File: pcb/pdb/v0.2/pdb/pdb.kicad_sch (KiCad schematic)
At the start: 29 parts, among them J1 UPDI, J3 Battery, J4 ESC A, J5 ESC B, J6 ESC C, J7 ESC D, J8 UART, J9 MPU, P1 Motor A, P2 Motor B, P3 Motor C, P4 Motor D, SW1 Control, SW2 Reset, U1 ATtiny814-SS, U2 LM317

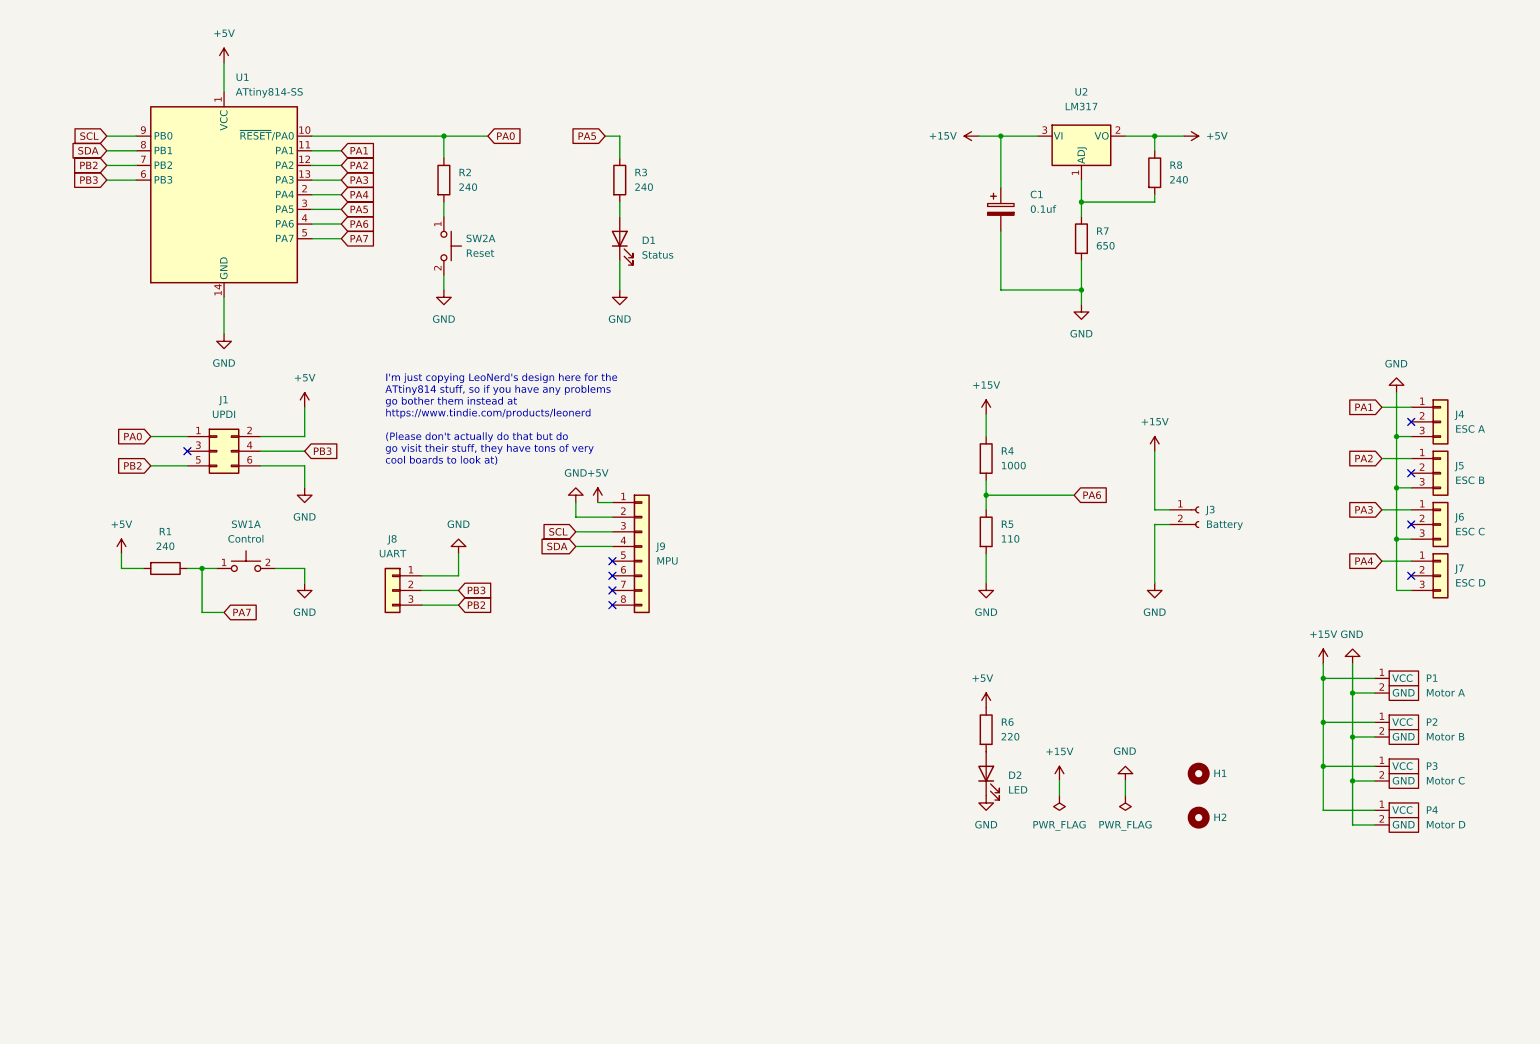
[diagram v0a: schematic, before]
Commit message: pcd: pdb: add USB port
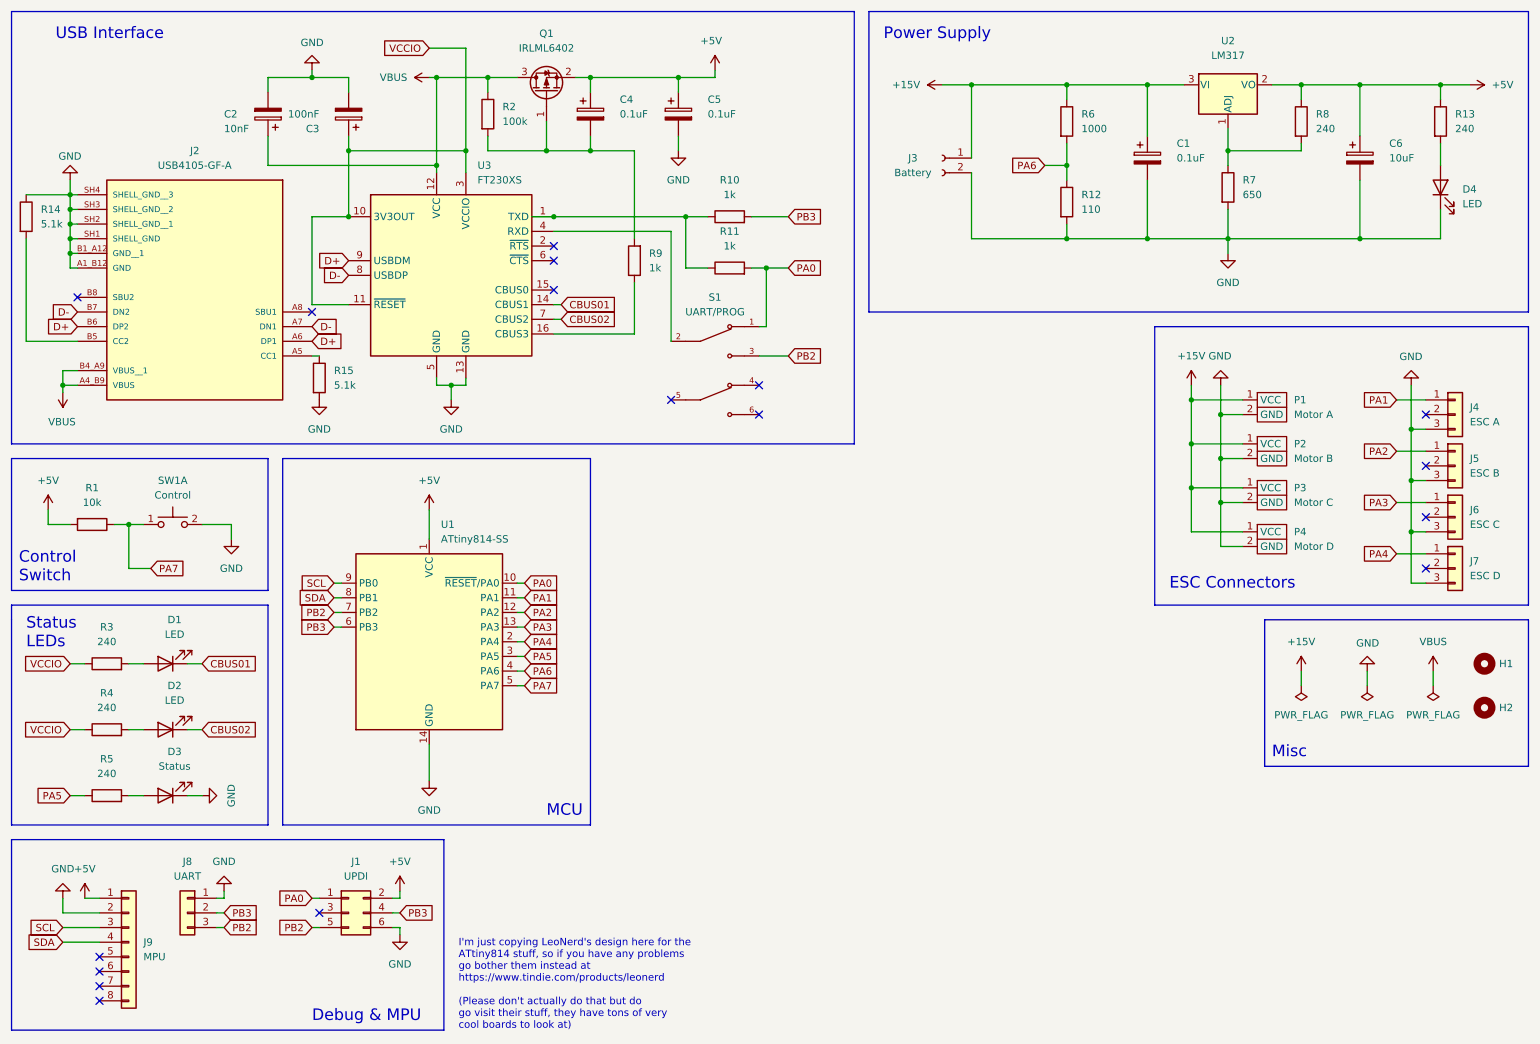
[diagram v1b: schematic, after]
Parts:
- removed SW2: Reset, Button_Switch_THT:SW_PUSH_6mm, symbol Switch:SW_Push_Dual_x2
- added C2: 10nF, Capacitor_SMD:C_1206_3216Metric, symbol Device:C_Polarized
- added C3: 100nF, Capacitor_SMD:C_1206_3216Metric, symbol Device:C_Polarized
- added C4, C5: 0.1uF, Capacitor_SMD:C_1206_3216Metric, symbol Device:C_Polarized
- added C6: 10uF, Capacitor_SMD:C_1206_3216Metric, symbol Device:C_Polarized
- added D3: Status, LED_SMD:LED_0805_2012Metric, symbol Device:LED
- added D4: LED, LED_SMD:LED_0805_2012Metric, symbol Device:LED
- added J2: USB4105-GF-A, USB4105:GCT_USB4105-GF-A, symbol USB4105-GF-A:USB4105-GF-A
- added Q1: IRLML6402, Package_TO_SOT_SMD:SOT-23, symbol Transistor_FET:IRLML6402
- added R10, R11, R9: 1k, Resistor_SMD:R_1206_3216Metric, symbol Device:R
- added R12: 110, Resistor_SMD:R_1206_3216Metric, symbol Device:R
- added R13: 240, Resistor_SMD:R_1206_3216Metric, symbol Device:R
- added R14, R15: 5.1k, Resistor_SMD:R_1206_3216Metric, symbol Device:R
- added S1: UART/PROG, Button_Switch_THT:SW_CuK_JS202011AQN_DPDT_Angled, symbol SLW-23775-5A-N-D:SLW-23775-5A-N-D
- added U3: FT230XS, FT230XS_R:SSOP16-0.635-5X4MM, symbol Interface_USB:FT230XS
- C1: value 0.1uf -> 0.1uF
- D1: value Status -> LED
- R1: value 240 -> 10k
- R2: value 240 -> 100k
- R4: value 1000 -> 240
- R5: value 110 -> 240
- R6: value 220 -> 1000
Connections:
- net +15V: now also R6.1; no longer R4.1
- net +5V: now also C4.1, C5.1, C6.1, Q1.2 (S), R13.1; no longer R6.1
- net GND: now also C2.2, C3.2, C5.2, C6.2, D3.1 (K), D4.1 (K), J2.A1_B12 (GND), J2.B1_A12 (GND__1), J2.SH1 (SHELL_GND), J2.SH2 (SHELL_GND__1), J2.SH3 (SHELL_GND__2), J2.SH4 (SHELL_GND__3), R12.2, R14.1, R15.2, U3.13 (GND), U3.5 (GND); no longer D1.1 (K), D2.1 (K), R5.2
- net PA0: now also R11.2, S1.1; no longer R2.1
- net PA5: now also R5.1; no longer R3.1
- net PA6: now also R6.2, R12.1; no longer R4.2, R5.1
- net PB2: now also S1.3
- net PB3: now also R10.2
- net at D2.2 (A): now also R4.2; no longer R6.2
- net at R2.2: now also C4.2, Q1.1 (G), R9.2
- new net: J2.A5 (CC1), R15.1
- new net: S1.2, U3.4 (RXD)
- new net: R9.1, U3.16 (CBUS3)
- new net: R10.1, R11.1, U3.1 (TXD)
- new net: D3.2 (A), R5.2
- new net: J2.B5 (CC2), R14.2
- new net: D4.2 (A), R13.2
- new net CBUS01: D1.1 (K), U3.14 (CBUS1)
- new net CBUS02: D2.1 (K), U3.7 (CBUS2)
- new net D+: J2.A6 (DP1), J2.B6 (DP2), U3.9 (USBDM)
- new net D-: J2.A7 (DN1), J2.B7 (DN2), U3.8 (USBDP)
- new net VBUS: C2.1, J2.A4_B9 (VBUS), J2.B4_A9 (VBUS__1), Q1.3 (D), R2.1, U3.12 (VCC)
- new net VCCIO: C3.1, R3.1, R4.1, U3.10 (3V3OUT), U3.11 (~{RESET}), U3.3 (VCCIO)
- no-connect marks 9 -> 17
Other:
- note added: "Control Switch"
- note added: "Debug & MPU"
- note added: "ESC Connectors"
- note added: "MCU"
- note added: "Misc"
- note added: "Power Supply"
- note added: "Status LEDs"
- note added: "USB Interface"
- moved on the sheet: C1, H1, H2, J1, J3, J4, J5, J6, J7, J8, J9, P1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
